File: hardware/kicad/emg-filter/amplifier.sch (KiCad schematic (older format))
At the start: 40 parts, among them U52 LM4565, U53 LM4565, U54 LM4565, U55 LM4565, U56 LM4565, U57 LM4565, U58 LM4565, U59 LM4565

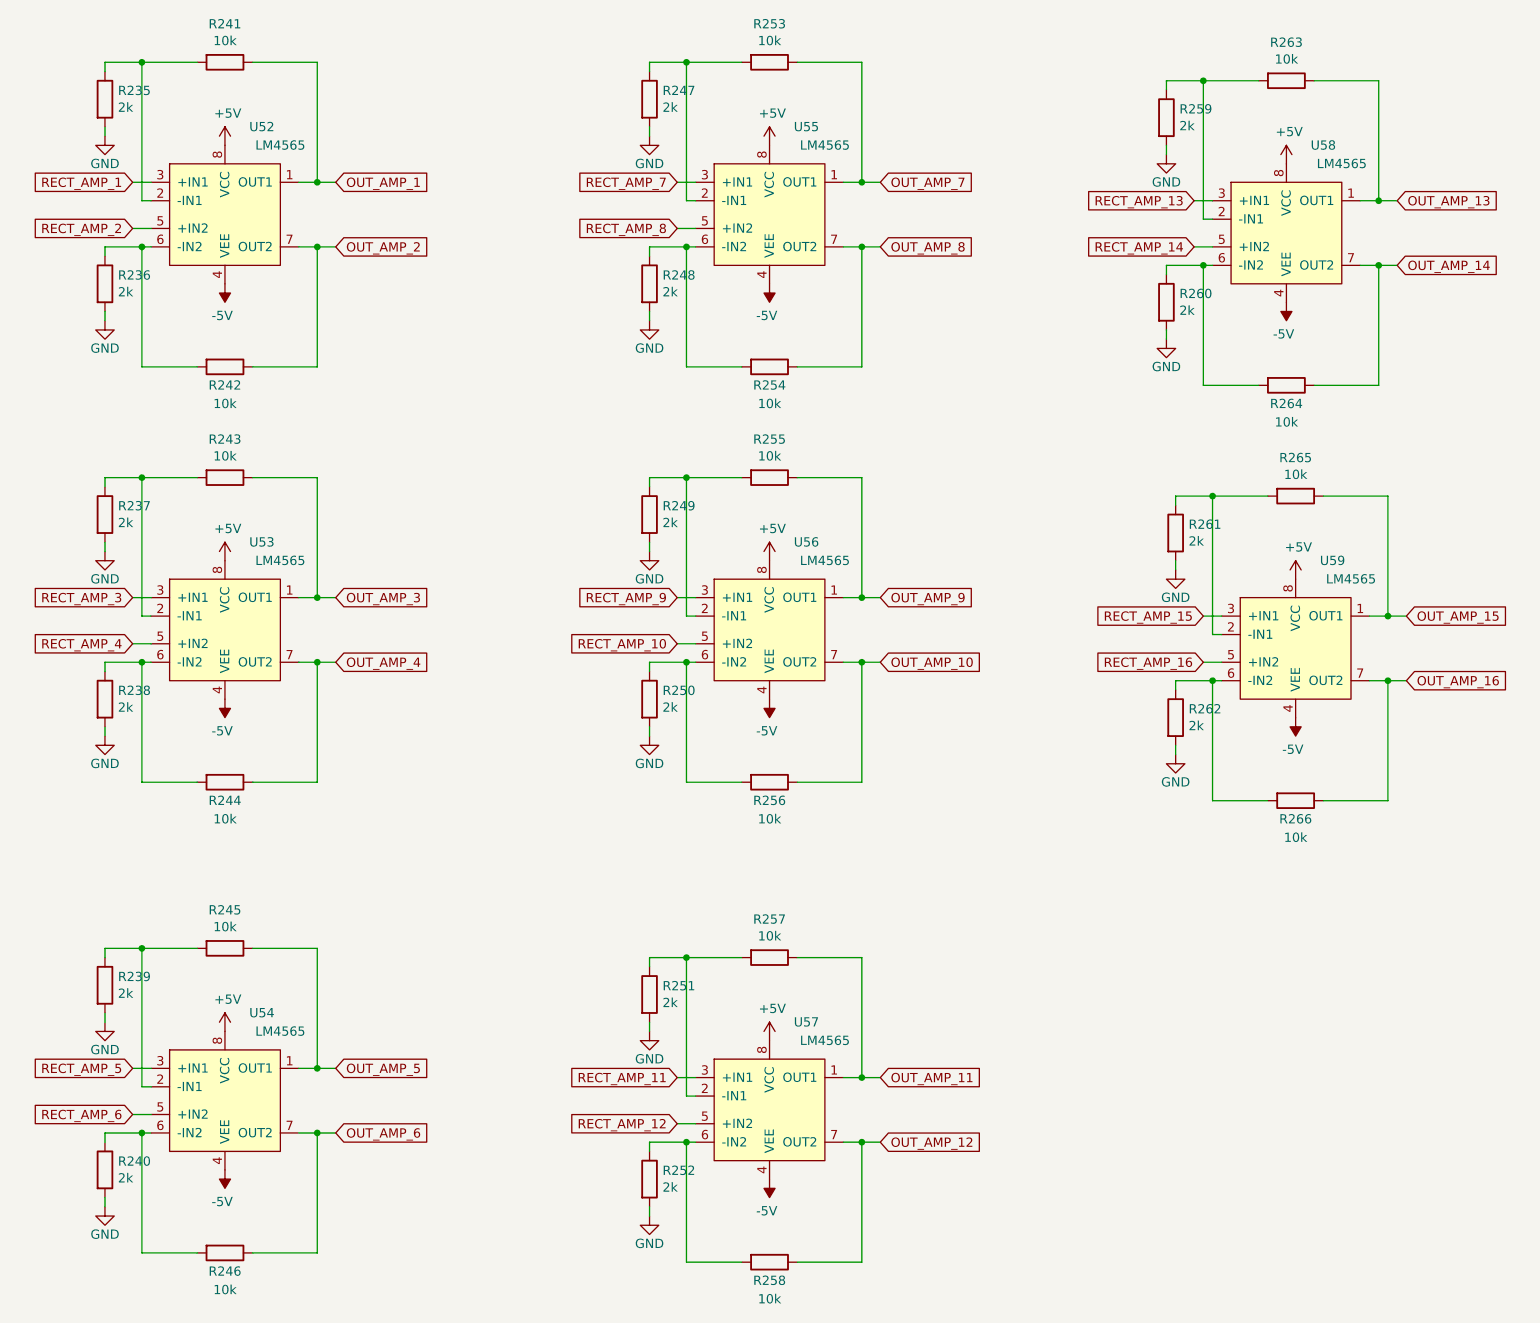
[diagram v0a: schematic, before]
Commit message: pi connector and adc
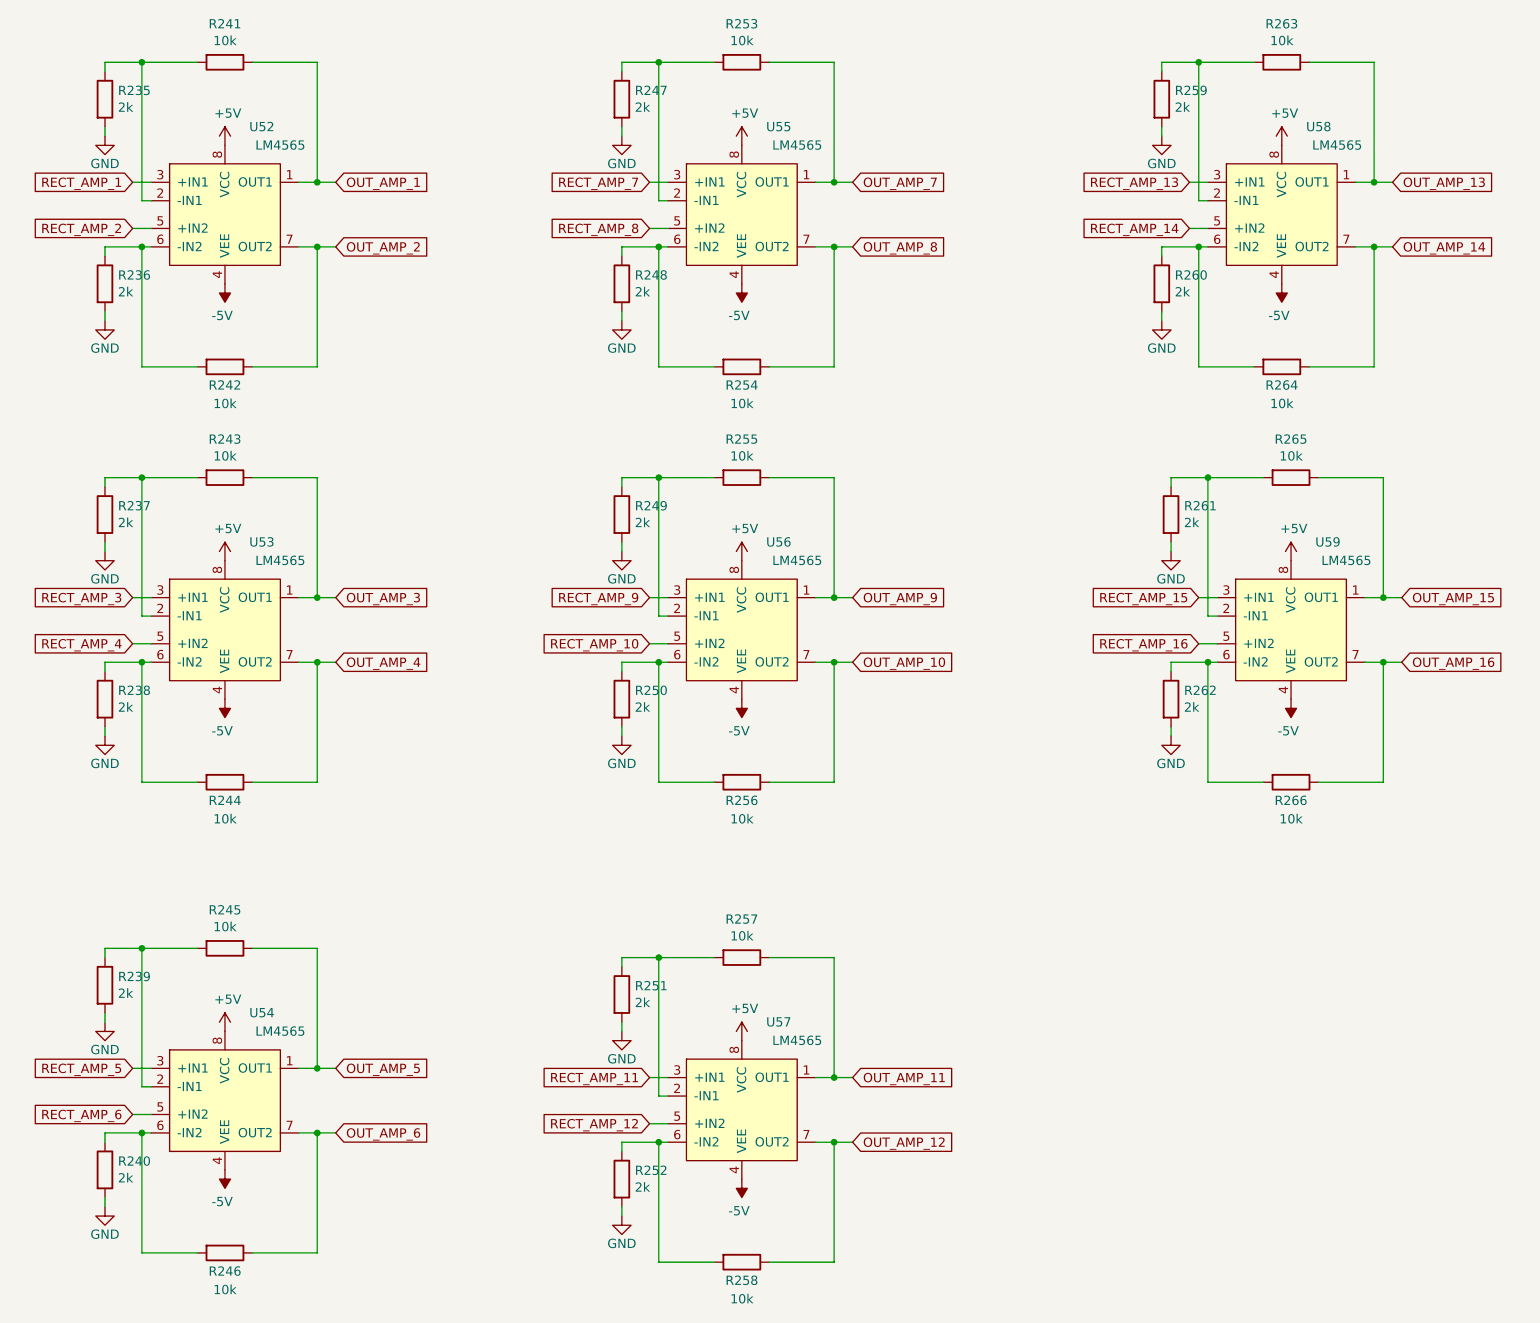
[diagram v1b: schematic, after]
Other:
- moved on the sheet: R247, R248, R249, R250, R251, R252, R253, R254, R255, R256, R257, R258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

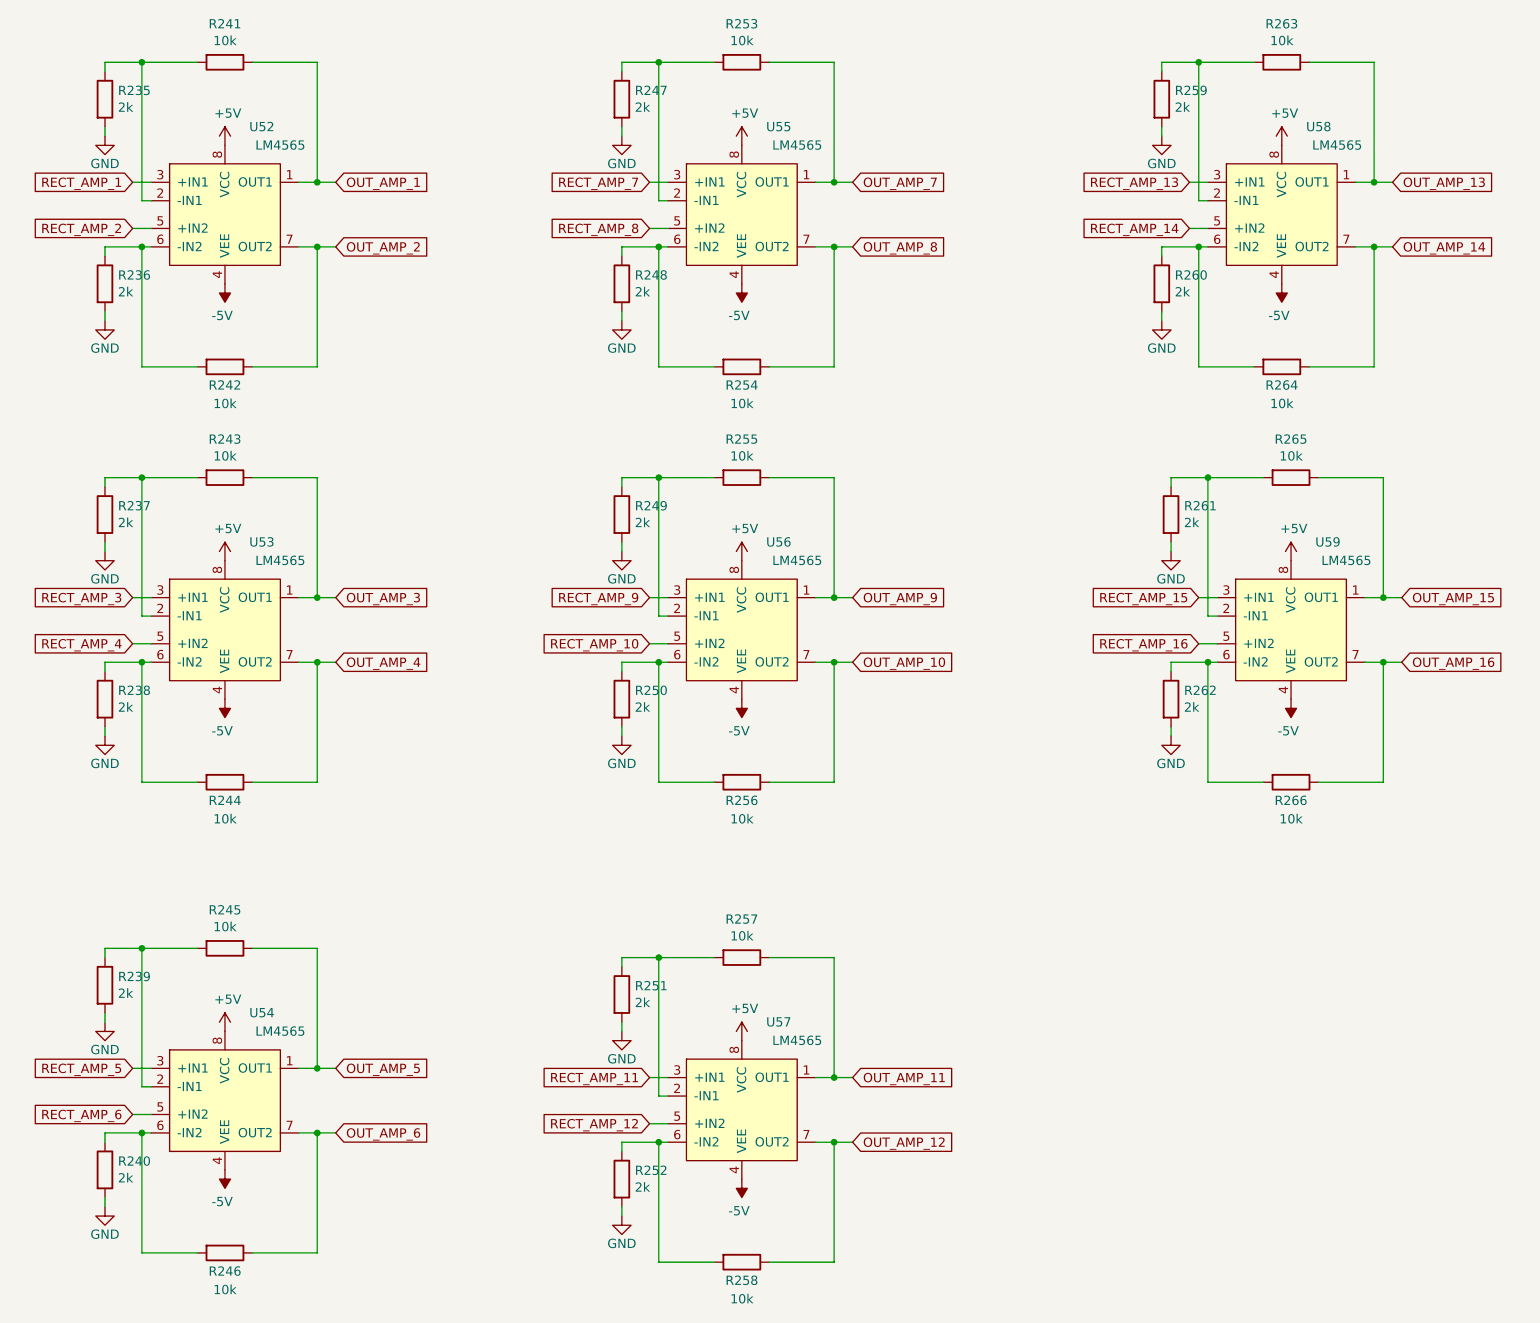
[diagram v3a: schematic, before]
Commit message: fixed rect labels
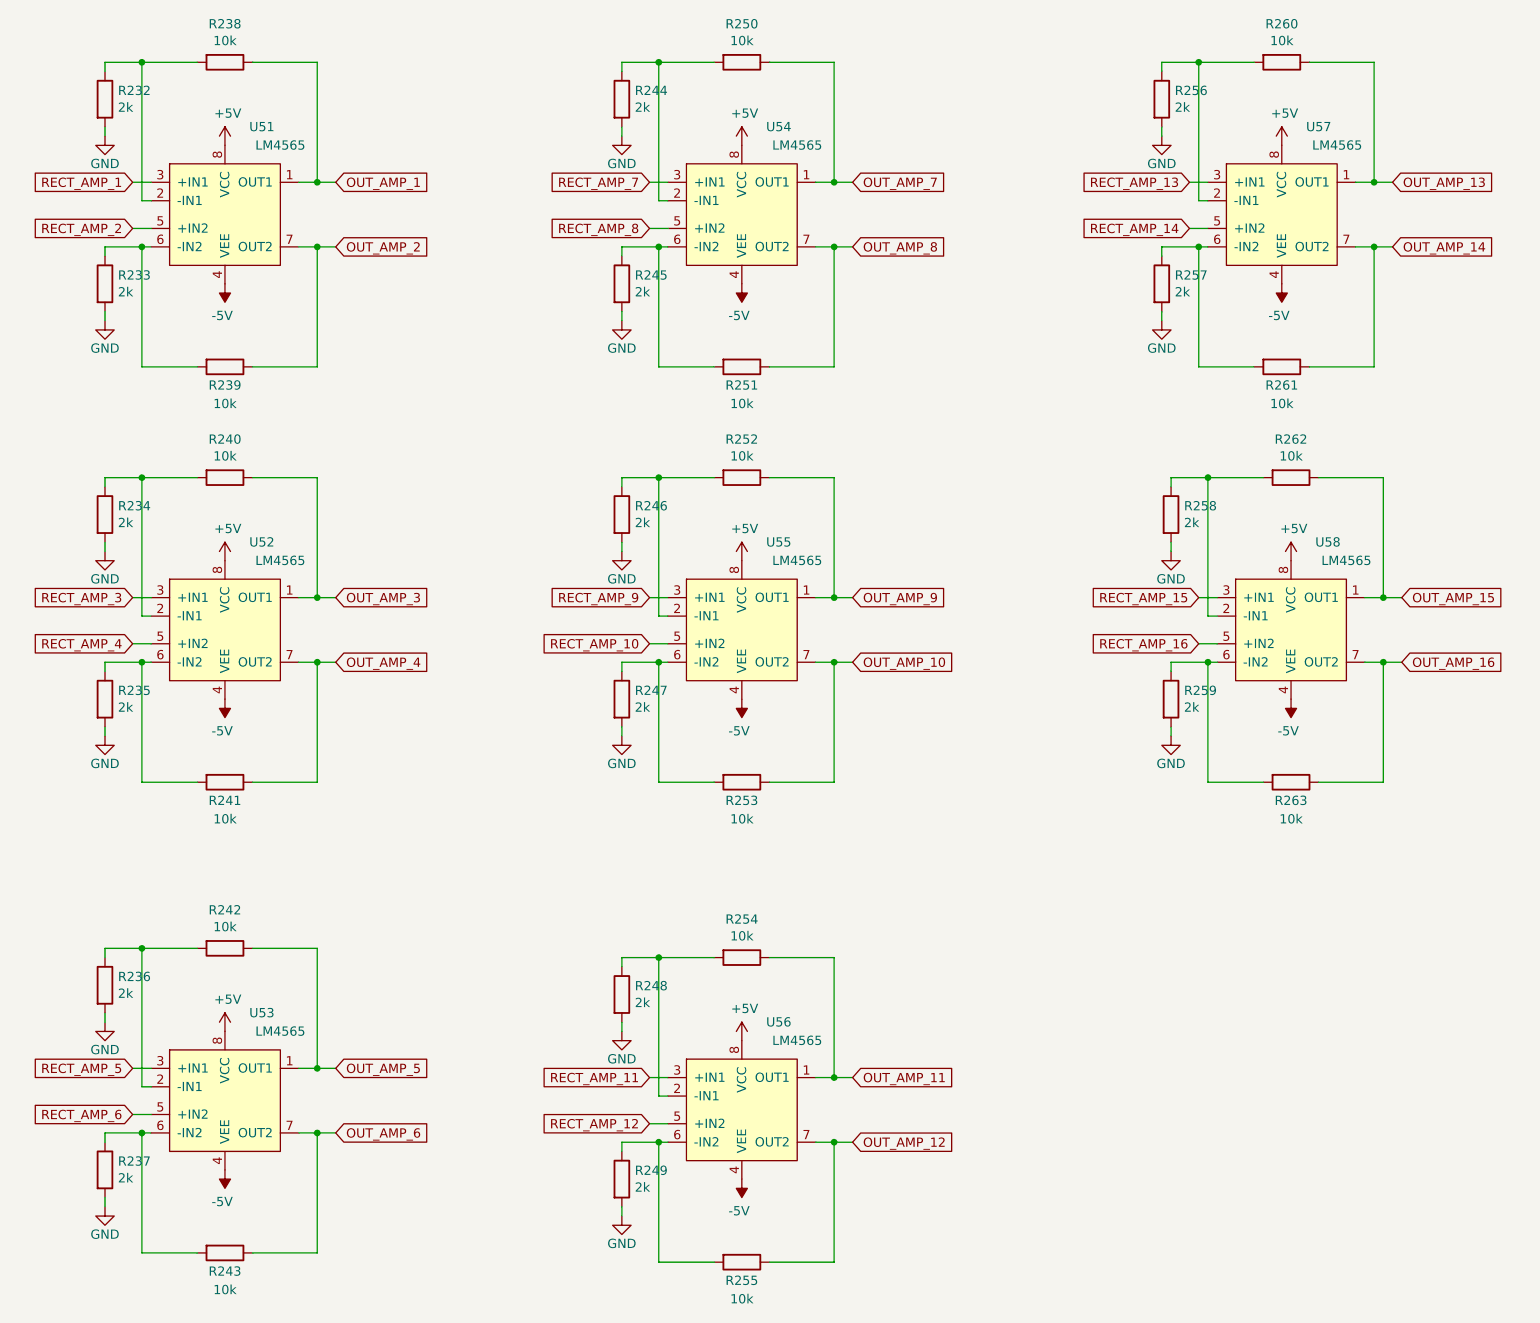
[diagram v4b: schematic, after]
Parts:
- renumbered R235 to R232, R236 to R233, R237 to R234, R238 to R235, R239 to R236, R240 to R237, R241 to R238, R242 to R239, R243 to R240, R244 to R241, R245 to R242, R246 to R243, R247 to R244, R248 to R245, R249 to R246, R250 to R247, R251 to R248, R252 to R249, R253 to R250, R254 to R251, R255 to R252, R256 to R253, R257 to R254, R258 to R255, R259 to R256, R260 to R257, R261 to R258, R262 to R259, R263 to R260, R264 to R261, R265 to R262, R266 to R263, U52 to U51, U53 to U52, U54 to U53, U55 to U54, U56 to U55, U57 to U56, U58 to U57, U59 to U58
